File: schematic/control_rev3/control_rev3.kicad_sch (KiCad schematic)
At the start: 142 parts, among them J28 Conn_02x07, J29 Conn_02x07, J30 Conn_01x16, J31 Conn_01x16, J32 Conn_02x05_Odd_Even, J33 MIDI, J34 Conn_02x02_Odd_Even, J36 GND, J37 AGND, J38 QWIIC, Q1 FDV303N, Q2 FDV303N, U12 TEENSY41, U13 LMR54406F, U14 LP2985A-5.0, U15 TPS7A2033, U16 LP5907-1.8, U17 MCP33131D, U18 74LV4051, U19 DAC8568, U20 74LV1T125, U21 74LV1T125, U22 74LV1T125, U23 74LV1T125, U24 PCM1808, U25 PCM1754, U26 OPA2277, U27 H11L1

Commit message: More minor fixes
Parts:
- C93: value 10uF -> 10uF Tantalum
- D2: value 5.1V -> 5.1V 3W
- R133, R134, R135, R136, R137: value 10K -> 10K 0.05%
- R138: value 20K -> 20K 0.05%
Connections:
- net +12VA: now also R129.1; no longer C54.2, C55.2, C56.2, C58.2, C59.2, C60.2, C61.2, C62.2, C64.2, C65.2, C66.2, C67.2, C68.1, C69.2, C70.2, C71.2, C72.2, C75.2, C76.2, C77.2, C78.2, C79.2, C80.2, C81.2, C82.2, C83.2, C84.2, C85.2, C86.2, C87.2, C88.2, C89.2, C90.2, C91.2, C93.2, J30.13 (Pin_13), J30.3 (Pin_3), J31.11 (Pin_11), J31.8 (Pin_8), J37.1, R124.2, R133.2, R136.1, R144.2, R200.2, U14.2 (GND), U15.2 (GND), U16.2 (GND), U17.4 (AIN-), U17.5 (GND), U18.6 (~{E}), U18.7 (VEE), U18.8 (GND), U19.1 (~{LDAC}), U19.14 (GND), U20.1 (~{OE}), U20.3 (GND), U21.1 (~{OE}), U21.3 (GND), U22.1 (~{OE}), U22.3 (GND), U24.10 (MD0), U24.11 (MD1), U24.12 (FMT), U24.2 (AGND), U25.12 (TEST), U25.13 (DEMP), U25.14 (MUTE), U25.15 (FMT), U25.4 (DGND), U25.9 (AGND), U26.5 (+)
- net ADC_MUX_A0: now also U12.7 (FlexIO2_17), U20.2 (A); no longer U12.6 (FlexIO2_10), U21.2 (A)
- net ADC_MUX_A1: now also U12.6 (FlexIO2_10), U21.2 (A); no longer U12.7 (FlexIO2_17), U20.2 (A)
- net at C53.1, C97.1, L1.2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: no longer R129.1
- new net GND: C54.2, C55.2, C56.2, C58.2, C59.2, C60.2, C61.2, C62.2, C64.2, C65.2, C66.2, C67.2, C68.1, C69.2, C70.2, C71.2, C72.2, C75.2, C76.2, C77.2, C78.2, C79.2, C80.2, C81.2, C82.2, C83.2, C84.2, C85.2, C86.2, C87.2, C88.2, C89.2, C90.2, C91.2, C93.2, J30.13 (Pin_13), J30.3 (Pin_3), J31.11 (Pin_11), J31.8 (Pin_8), J37.1, R124.2, R133.2, R136.1, R144.2, R200.2, U14.2 (GND), U15.2 (GND), U16.2 (GND), U17.4 (AIN-), U17.5 (GND), U18.6 (~{E}), U18.7 (VEE), U18.8 (GND), U19.1 (~{LDAC}), U19.14 (GND), U20.1 (~{OE}), U20.3 (GND), U21.1 (~{OE}), U21.3 (GND), U22.1 (~{OE}), U22.3 (GND), U24.10 (MD0), U24.11 (MD1), U24.12 (FMT), U24.2 (AGND), U25.12 (TEST), U25.13 (DEMP), U25.14 (MUTE), U25.15 (FMT), U25.4 (DGND), U25.9 (AGND), U26.5 (+)
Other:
- note added: "Place 100Ω resistors close to Teensy 4.1"
- note added: "Place R112 close to U17"
- note added: "Place R144 close to U17"
- note added: "U14 pin 3 keeps analog power off until end of Teensy powerup sequence"
- note added: "U16 pin 3 assures simultaneous AVDD and VREF startup for U17. See note in MCP33131D datasheet on page 29 near 5.2.1."
- note added: "Use PCB copper to improve D2 thermal dissipation"
- moved on the sheet: C53, C62, C79, C97, D2, L1, R128, R129, R133, R134

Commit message: Another minor fix
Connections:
- net ADC_SCK: no longer R106.1, U12.10 (SPI0_CS)
- new net DAC_CS: R106.1, U12.10 (SPI0_CS)
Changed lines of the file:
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@@
     (effects (font (size 1.27 1.27)) (justify left bottom))
   )
-  (label "ADC_SCK" (at 72.39 186.69 0) (fields_autoplaced)
+  (label "DAC_CS" (at 72.39 186.69 0) (fields_autoplaced)
     (effects (font (size 1.27 1.27)) (justify left bottom))
   )

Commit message: Update schematics, CC BY-SA with attribution to mxmxmx
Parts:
- R121, R124: value 4.7K -> 4.7K 1%
- R125: value 11K -> 11K 1%
- R126: value 5.11K -> 5.11K 1%
- R127, R128: value 22K -> 22K 1%
- R129, R130: value 150K -> 150K 1%
- R200, R201, R202: Field4 (none) -> DNP
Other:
- note added: "Place R113 close to U24"
- note added: "Use precision resistors for R133-R138. Don't be cheap! Accurate reference, offset, bias voltages are worth the small expense of quality parts."
- company: (none) -> Copyright 2024 Paul Stoffregen, mxmxmx - CC BY-SA 4.0
- title: (none) -> O_C T4.1  Ornament and Crime optimized for Teensy 4.1
- moved on the sheet: C67, C68, L3, R136, TP12, TP13, U20, U21, U22, U26C

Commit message: Fix R118 on control board schematic
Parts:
- renumbered R119 to R118
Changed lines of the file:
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@@
   (symbol (lib_id "Device:R_US") (at 295.91 490.22 90) (unit 1)
     (in_bom yes) (on_board yes) (dnp no) (fields_autoplaced)
-    (property "Reference" "R119" (at 295.91 483.87 90)
+    (property "Reference" "R118" (at 295.91 483.87 90)
       (effects (font (size 1.27 1.27)))
     )
@@
       (project "control_rev3"
         (path "/f666d35b-d6a1-4bcd-8ace-0f923f42ac67"
-          (reference "R119") (unit 1)
+          (reference "R118") (unit 1)
         )
       )

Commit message: converted gerbers to kicad_pcb files and added/customized footprints. generated new gerbers for testing and comparison.
still a few nuisance DRC warnings, mostly footprint quirks and silkscreen overlap, etc.

pcb files expect the included Custom_Footprints library to be added to the project
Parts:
- C52, C53, C54, C55, C56, C57, C58, C59, C60, C61, C62, C63, C64, C65, C66, C67, C68, C69, C70, C71, C72, C73, C74, C75, C76, C77, C78, C79, C80, C81, C82, C83, C84, C85, C86, C87, C88, C89, C90, C91, C92, C94: footprint (none) -> Custom_Footprints:C_0805_2012Metric_Pad1.18x1.45mm_HandSolder_rectpads
- C93, C95, C96, C97: footprint (none) -> Custom_Footprints:C_1206_3216Metric_Pad1.33x1.80mm_HandSolder_rectpads
- D1: footprint (none) -> Custom_Footprints:Diode_Bridge_reduced
- D2, D3, D4: footprint (none) -> Custom_Footprints:D_SMB_Handsoldering_rectpads
- F1: footprint (none) -> Custom_Footprints:Fuse_1812_4532Metric_Pad1.30x3.40mm_HandSolder_rectpads
- J28, J29: footprint (none) -> Custom_Footprints:PinSocket_2x07_P2.54mm_Vertical_reduced
- J30, J31: footprint (none) -> Custom_Footprints:PinSocket_1x16_P2.54mm_Vertical_reduced
- J32: footprint (none) -> Connector_IDC:IDC-Header_2x05_P2.54mm_Vertical
- J33: footprint (none) -> Custom_Footprints:PinHeader_1x04_P2.54mm_Vertical_reduced
- J34: footprint (none) -> Connector_PinHeader_2.54mm:PinHeader_2x02_P2.54mm_Vertical
- J38: footprint (none) -> Custom_Footprints:JST_SMD_1.0mm-4
- L1, L3: footprint (none) -> Custom_Footprints:L_0805_2012Metric_rectpads
- L2: footprint (none) -> Custom_Footprints:L_Abracon_ASPI-4030S_rectpads
- Q1, Q2: footprint (none) -> Custom_Footprints:SOT-23-3_rectpads
- R103, R104, R105, R106, R107, R108, R109, R110, R111, R112, R113, R114, R115, R116, R117, R118, R119, R120, R121, R122, R123, R124, R125, R126, R127, R128, R129, R130, R131, R132, R133, R134, R135, R136, R137, R138, R144, R200, R201, R202: footprint (none) -> Custom_Footprints:R_0805_2012Metric_Pad1.20x1.40mm_HandSolder_rectpads
- R139, R140, R141, R142, R143: footprint (none) -> Custom_Footprints:R_1206_3216Metric_Pad1.30x1.75mm_HandSolder_rectpads
- U12: footprint (none) -> Custom_Footprints:Teensy41
- U13: footprint (none) -> Custom_Footprints:SOT-23-6_rectpads
- U14, U15, U16, U20, U21, U22, U23: footprint Package_TO_SOT_SMD:SOT-23-5 -> Custom_Footprints:SOT-23-5_reducedpads
- U17: footprint (none) -> Custom_Footprints:MSOP-10_3x3mm_P0.5mm_silkscreen+footprint
- U18, U19, U25: footprint (none) -> Custom_Footprints:TSSOP-16_4.4x5mm_P0.65mm_silkscreen
- U24: footprint (none) -> Custom_Footprints:TSSOP-14_4.4x5mm_P0.65mm_silkscreen
- U26: footprint (none) -> Custom_Footprints:SOIC-8_3.9x4.9mm_P1.27mm_shiftedpads
- U27: footprint (none) -> Package_DIP:DIP-6_W7.62mm

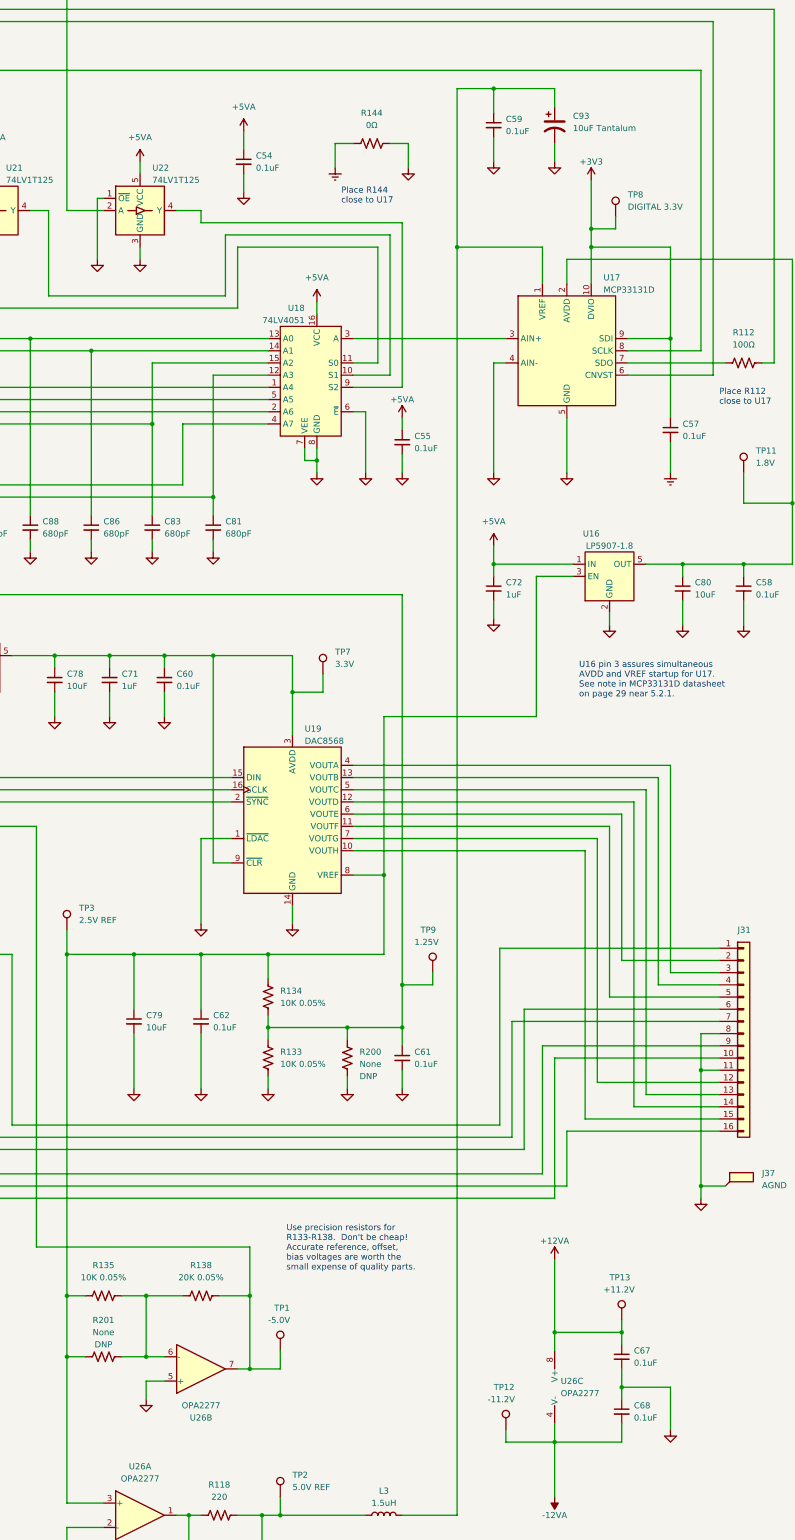
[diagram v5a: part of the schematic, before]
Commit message: added D6 per Paul's recommendation, to help protect U17
reduced pads on ADC footprint to help prevent solder bridging

updated a few footprint silkscreens to look more like original rev3 board

generated updated gerber zip files

TODO: update IC pads to match more closely to original rev3 board if it makes soldering easier
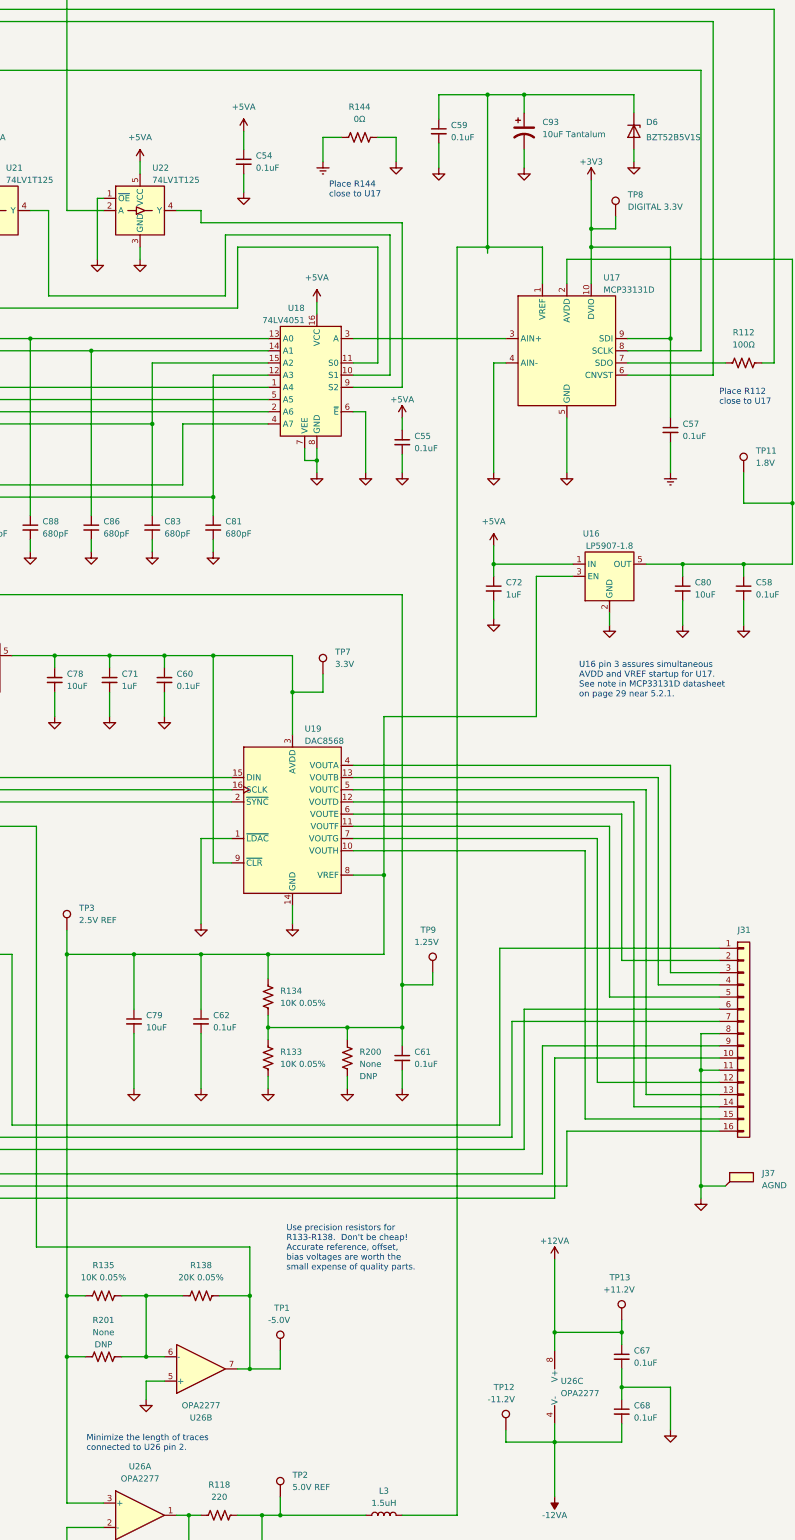
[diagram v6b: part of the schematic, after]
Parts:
- added D6: BZT52B5V1S, Custom_Footprints:D_SOD-323F_rectpads, symbol Device:D_Zener
- J32: footprint Connector_IDC:IDC-Header_2x05_P2.54mm_Vertical -> Custom_Footprints:IDC-Header_2x05_P2.54mm_Vertical_reduced
- J34: footprint Connector_PinHeader_2.54mm:PinHeader_2x02_P2.54mm_Vertical -> Custom_Footprints:PinHeader_2x02_P2.54mm_Vertical_symmetric
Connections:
- net GND: now also D6.2 (A)
- net at C59.1, C93.1, L3.2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: now also D6.1 (K)
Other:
- note added: "Minimize the length of traces connected to U26 pin 2."
- moved on the sheet: C59, C93, R144
